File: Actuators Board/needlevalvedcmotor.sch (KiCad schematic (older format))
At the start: 32 parts, among them J10 Conn_01x02_Male, J9 Conn_01x02_Male, Q1 MMDT2222A

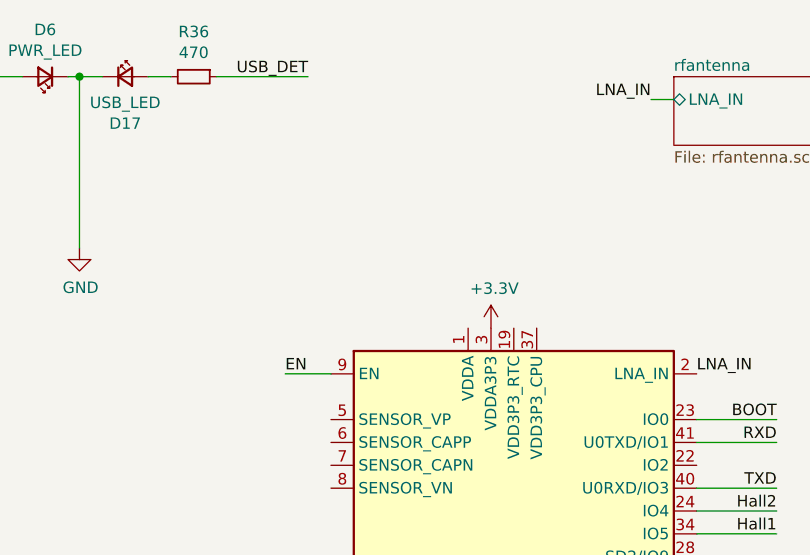
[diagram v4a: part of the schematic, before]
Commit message: Connected 3.3V to ESP32 according to schematic
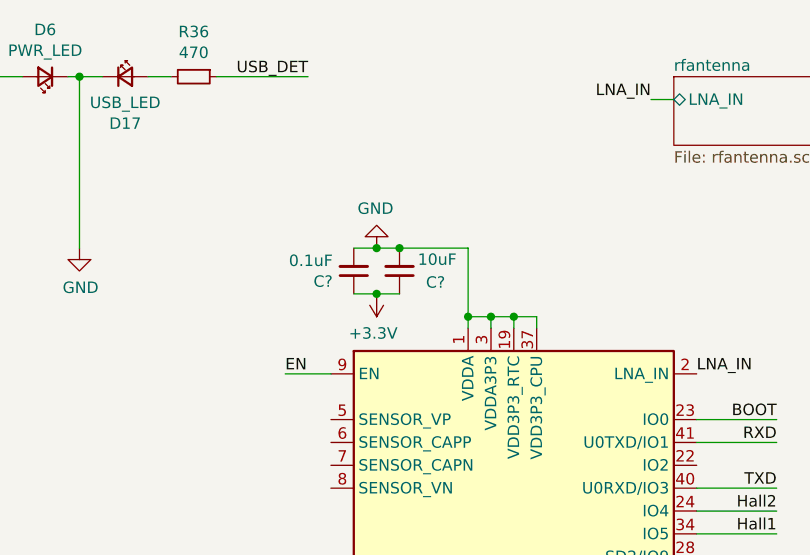
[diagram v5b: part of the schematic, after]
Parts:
- added C?: 10uF, symbol Device:C_Small
- added C?: 0.1uF, symbol Device:C_Small
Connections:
- net +3V3: now also C?.1, C?.1; no longer U?.3 (VDDA3P3), U?.4 (VDDA3P3)
- net GND: now also U?.1 (VDDA), U?.19 (VDD3P3_RTC), U?.3 (VDDA3P3), U?.37 (VDD3P3_CPU), U?.4 (VDDA3P3), U?.43 (VDDA), U?.46 (VDDA), C?.2, C?.2
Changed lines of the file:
@@
 $EndDescr
-$Comp
-L power:+3.3V #PWR020
-U 1 1 5DA60792
-P 4100 1950
-F 0 "#PWR020" H 4100 1800 50  0001 C CNN
-F 1 "+3.3V" H 4115 2123 50  0000 C CNN
-F 2 "" H 4100 1950 50  0001 C CNN
-F 3 "" H 4100 1950 50  0001 C CNN
-	1    4100 1950
-	1    0    0    -1
-$EndComp
 $Comp
 L power:GND #PWR021
@@
 Text Label 4700 6900 0    50   ~ 0
 CAN_RX
+$Comp
+L power:+3.3V #PWR?
+U 1 1 61AA6780
+P 3600 1800
+F 0 "#PWR?" H 3600 1650 50  0001 C CNN
+F 1 "+3.3V" H 3615 1973 50  0000 C CNN
+F 2 "" H 3600 1800 50  0001 C CNN
+F 3 "" H 3600 1800 50  0001 C CNN
+	1    3600 1800
+	-1   0    0    1
+$EndComp
+$Comp
+L Device:C_Small C?
+U 1 1 61AA6786
+P 3700 1700
+F 0 "C?" H 3500 1750 50  0000 L CNN
+F 1 "10uF" H 3450 1650 50  0000 L CNN
+F 2 "" H 3700 1700 50  0001 C CNN
+F 3 "~" H 3700 1700 50  0001 C CNN
+	1    3700 1700
+	-1   0    0    1
+$EndComp
+$Comp
+L Device:C_Small C?
+U 1 1 61AA678C
+P 3500 1700
+F 0 "C?" H 3592 1746 50  0000 L CNN
+F 1 "0.1uF" H 3592 1655 50  0000 L CNN
+F 2 "" H 3500 1700 50  0001 C CNN
+F 3 "~" H 3500 1700 50  0001 C CNN
+	1    3500 1700
+	-1   0    0    1
+$EndComp
+Wire Wire Line
+	3700 1800 3600 1800
+Wire Wire Line
+	3700 1600 3600 1600
+$Comp
+L power:GND #PWR?
+U 1 1 61AA6794
+P 3600 1600
+F 0 "#PWR?" H 3600 1350 50  0001 C CNN
+F 1 "GND" H 3605 1427 50  0000 C CNN
+F 2 "" H 3600 1600 50  0001 C CNN
+F 3 "" H 3600 1600 50  0001 C CNN
+	1    3600 1600
+	-1   0    0    1
+$EndComp
+Connection ~ 3600 1600
+Wire Wire Line
+	3600 1600 3500 1600
+Connection ~ 3600 1800
+Wire Wire Line
+	3600 1800 3500 1800
+Wire Wire Line
+	3700 1600 4000 1600
+Wire Wire Line
+	4000 1600 4000 1900
+Connection ~ 3700 1600
+Wire Wire Line
+	4000 1900 4100 1900
+Wire Wire Line
+	4100 1900 4100 1950
+Connection ~ 4000 1900
+Wire Wire Line
+	4000 1900 4000 1950
+Wire Wire Line
+	4100 1900 4200 1900
+Wire Wire Line
+	4200 1900 4200 1950
+Connection ~ 4100 1900
+Wire Wire Line
+	4200 1900 4300 1900
+Wire Wire Line
+	4300 1900 4300 1950
+Connection ~ 4200 1900
 $EndSCHEMATC

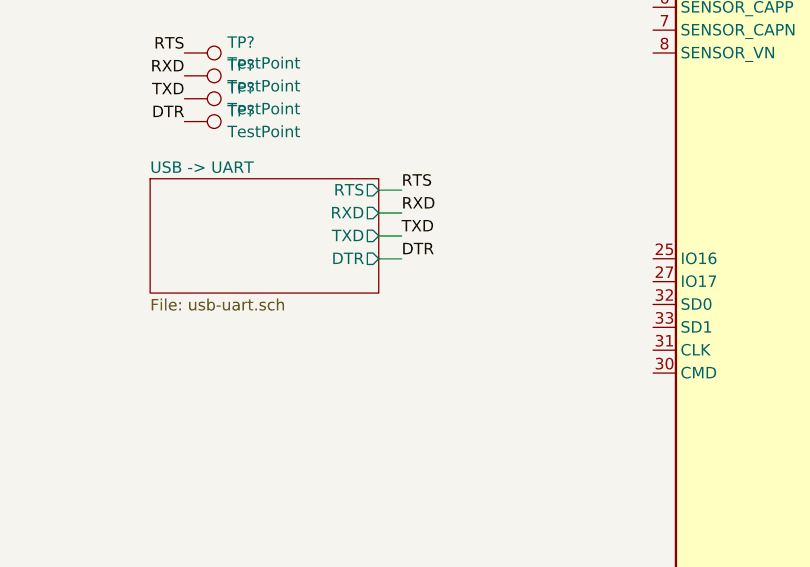
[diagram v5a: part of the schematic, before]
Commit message: Connected 3.3V output from USB-UART converter
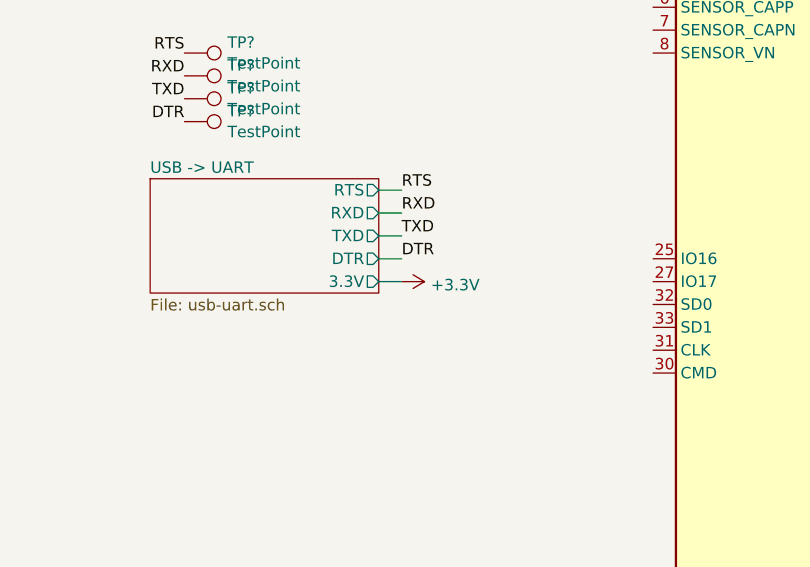
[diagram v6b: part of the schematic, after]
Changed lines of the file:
@@
 F4 "TXD" O R 2200 3450 50
 F5 "DTR" O R 2200 3550 50
+F6 "3.3V" O R 2200 3650 50
 $EndSheet
 $Comp
@@
 	4300 1900 4300 1950
 Connection ~ 4200 1900
+Wire Wire Line
+	2200 3650 2300 3650
+$Comp
+L power:+3.3V #PWR?
+U 1 1 61A70159
+P 2300 3650
+F 0 "#PWR?" H 2300 3500 50  0001 C CNN
+F 1 "+3.3V" V 2315 3778 50  0000 L CNN
+F 2 "" H 2300 3650 50  0001 C CNN
+F 3 "" H 2300 3650 50  0001 C CNN
+	1    2300 3650
+	0    1    1    0
+$EndComp
 $EndSCHEMATC

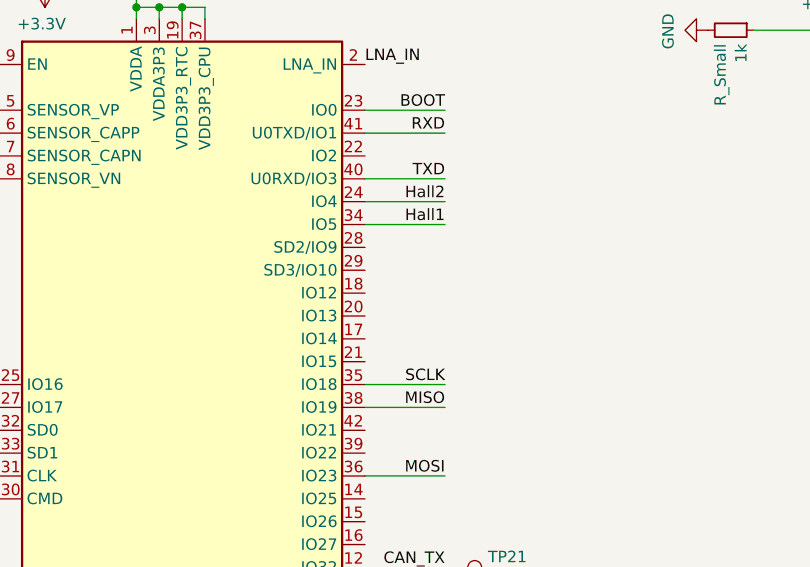
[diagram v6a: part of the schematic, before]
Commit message: Connected H bridge PWM pin to ESP32
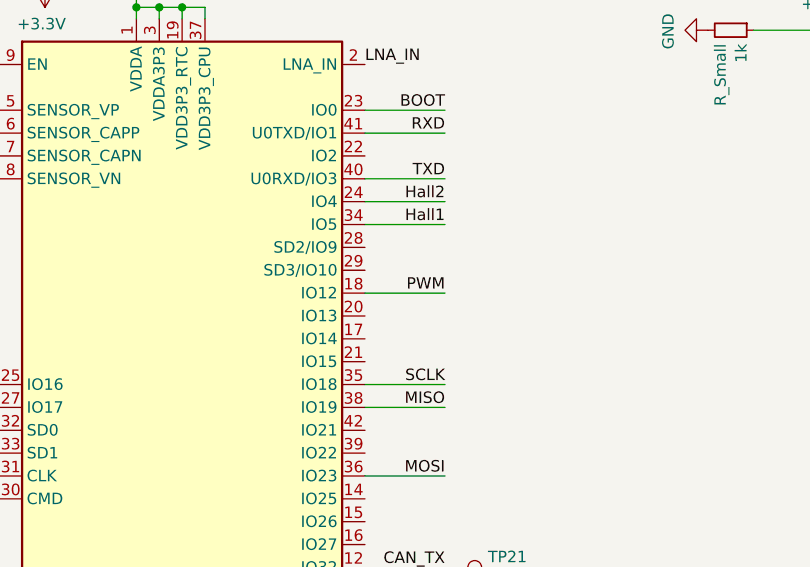
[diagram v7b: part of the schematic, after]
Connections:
- net PWM: now also U?.18 (IO12)
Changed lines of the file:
@@
 	0    1    1    0
 $EndComp
+Wire Wire Line
+	5000 3150 5350 3150
+Text Label 5350 3150 2    50   ~ 0
+PWM
 $EndSCHEMATC

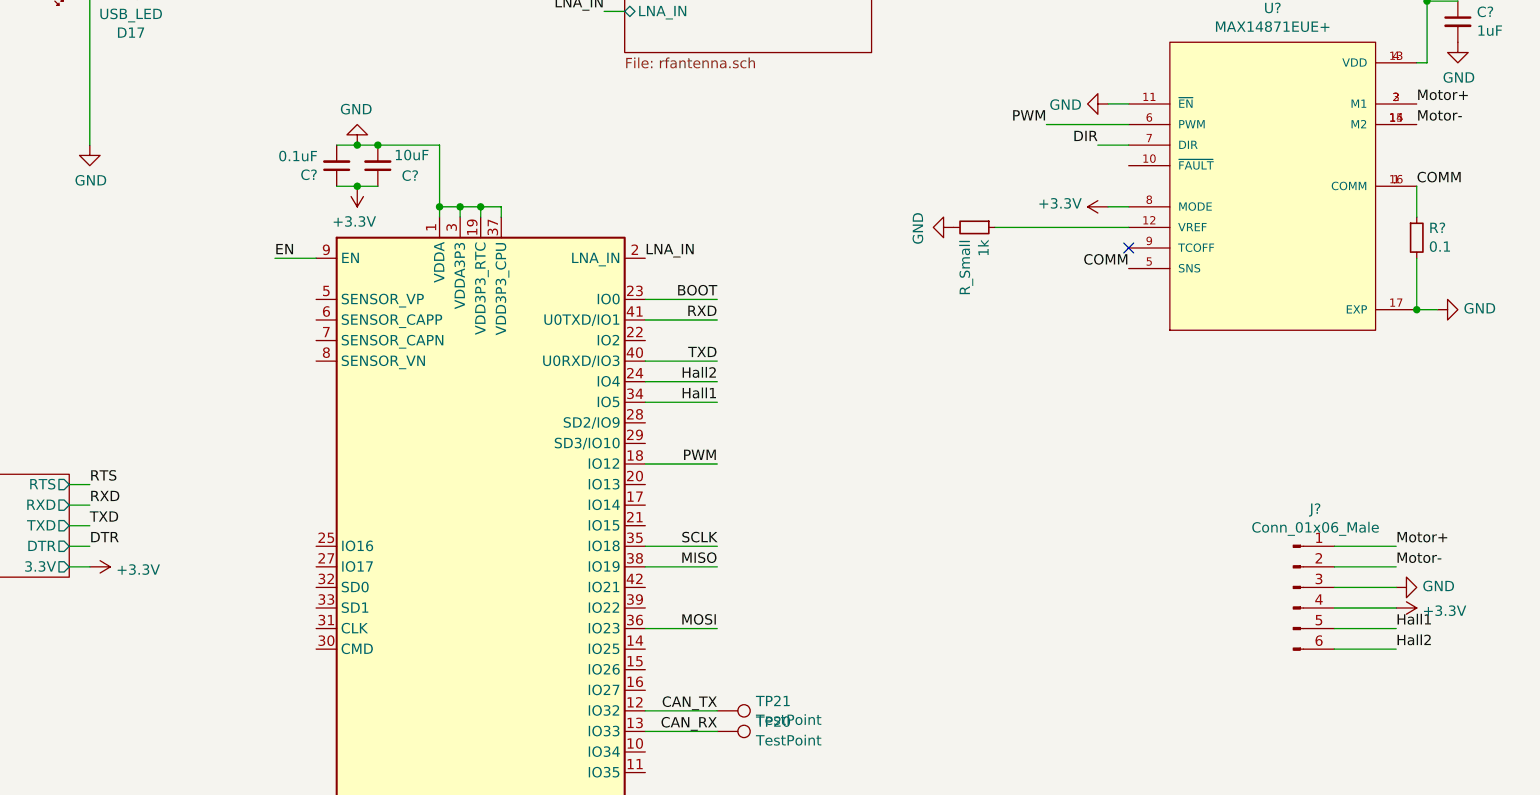
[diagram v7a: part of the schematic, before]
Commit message: Added test points to needle valve motor board
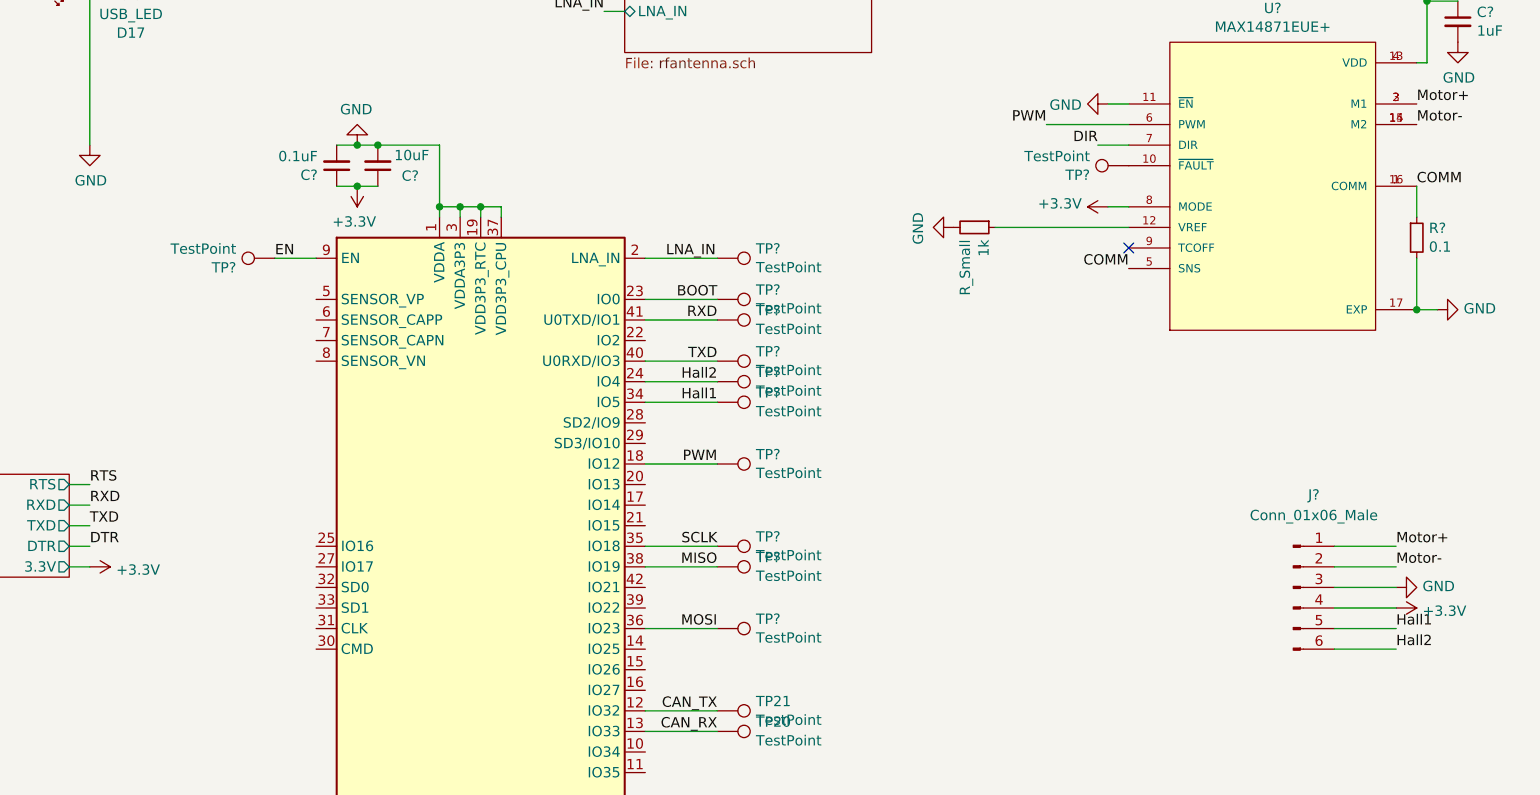
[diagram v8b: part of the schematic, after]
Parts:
- added TP? (x12): TestPoint, symbol Connector:TestPoint
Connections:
- net BOOT: now also TP?.1
- net EN: now also TP?.1
- net Hall1: now also TP?.1
- net Hall2: now also TP?.1
- net LNA_IN: now also TP?.1
- net MISO: now also TP?.1
- net MOSI: now also TP?.1
- net PWM: now also TP?.1
- net RXD: now also TP?.1
- net SCLK: now also TP?.1
- net TXD: now also TP?.1
- net at U?.10 (~FAULT): now also TP?.1
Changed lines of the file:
@@
 U 1 1 6194A5D2
 P 8150 3750
-F 0 "J?" H 8258 4131 50  0000 C CNN
-F 1 "Conn_01x06_Male" H 8258 4040 50  0000 C CNN
+F 0 "J?" H 8250 4200 50  0000 C CNN
+F 1 "Conn_01x06_Male" H 8250 4100 50  0000 C CNN
 F 2 "" H 8150 3750 50  0001 C CNN
 F 3 "~" H 8150 3750 50  0001 C CNN
@@
 Wire Wire Line
 	6700 2000 7350 2000
-Text Label 8650 3550 0    50   ~ 0
-Motor+
 Wire Wire Line
 	8350 3550 8650 3550
@@
 F2 "LNA_IN" B L 4900 950 50
 $EndSheet
-Text Label 5000 2150 0    50   ~ 0
+Text Label 5100 2150 0    50   ~ 0
 LNA_IN
 Text Label 4800 950  2    50   ~ 0
@@
 Text Label 5350 3150 2    50   ~ 0
 PWM
+Text Label 8650 3550 0    50   ~ 0
+Motor+
+$Comp
+L Connector:TestPoint TP?
+U 1 1 61B1B7B5
+P 5350 2350
+F 0 "TP?" V 5304 2538 50  0000 L CNN
+F 1 "TestPoint" V 5395 2538 50  0000 L CNN
+F 2 "" H 5550 2350 50  0001 C CNN
+F 3 "~" H 5550 2350 50  0001 C CNN
+	1    5350 2350
+	0    1    1    0
+$EndComp
+$Comp
+L Connector:TestPoint TP?
+U 1 1 61B1BFB6
+P 5350 2450
+F 0 "TP?" V 5304 2638 50  0000 L CNN
+F 1 "TestPoint" V 5395 2638 50  0000 L CNN
+F 2 "" H 5550 2450 50  0001 C CNN
+F 3 "~" H 5550 2450 50  0001 C CNN
+	1    5350 2450
+	0    1    1    0
+$EndComp
+$Comp
+L Connector:TestPoint TP?
+U 1 1 61B22D1D
+P 5350 2650
+F 0 "TP?" V 5304 2838 50  0000 L CNN
+F 1 "TestPoint" V 5395 2838 50  0000 L CNN
+F 2 "" H 5550 2650 50  0001 C CNN
+F 3 "~" H 5550 2650 50  0001 C CNN
+	1    5350 2650
+	0    1    1    0
+$EndComp
+$Comp
+L Connector:TestPoint TP?
+U 1 1 61B26251
+P 5350 2750
+F 0 "TP?" V 5304 2938 50  0000 L CNN
+F 1 "TestPoint" V 5395 2938 50  0000 L CNN
+F 2 "" H 5550 2750 50  0001 C CNN
+F 3 "~" H 5550 2750 50  0001 C CNN
+	1    5350 2750
+	0    1    1    0
+$EndComp
+$Comp
+L Connector:TestPoint TP?
+U 1 1 61B29519
+P 5350 2850
+F 0 "TP?" V 5304 3038 50  0000 L CNN
+F 1 "TestPoint" V 5395 3038 50  0000 L CNN
+F 2 "" H 5550 2850 50  0001 C CNN
+F 3 "~" H 5550 2850 50  0001 C CNN
+	1    5350 2850
+	0    1    1    0
+$EndComp
+$Comp
+L Connector:TestPoint TP?
+U 1 1 61B2CAF9
+P 5350 3150
+F 0 "TP?" V 5304 3338 50  0000 L CNN
+F 1 "TestPoint" V 5395 3338 50  0000 L CNN
+F 2 "" H 5550 3150 50  0001 C CNN
+F 3 "~" H 5550 3150 50  0001 C CNN
+	1    5350 3150
+	0    1    1    0
+$EndComp
+$Comp
+L Connector:TestPoint TP?
+U 1 1 61B2FF39
+P 5350 3550
+F 0 "TP?" V 5304 3738 50  0000 L CNN
+F 1 "TestPoint" V 5395 3738 50  0000 L CNN
+F 2 "" H 5550 3550 50  0001 C CNN
+F 3 "~" H 5550 3550 50  0001 C CNN
+	1    5350 3550
+	0    1    1    0
+$EndComp
+$Comp
+L Connector:TestPoint TP?
+U 1 1 61B33316
+P 5350 3950
+F 0 "TP?" V 5304 4138 50  0000 L CNN
+F 1 "TestPoint" V 5395 4138 50  0000 L CNN
+F 2 "" H 5550 3950 50  0001 C CNN
+F 3 "~" H 5550 3950 50  0001 C CNN
+	1    5350 3950
+	0    1    1    0
+$EndComp
+$Comp
+L Connector:TestPoint TP?
+U 1 1 61B3A0CE
+P 5350 3650
+F 0 "TP?" V 5304 3838 50  0000 L CNN
+F 1 "TestPoint" V 5395 3838 50  0000 L CNN
+F 2 "" H 5550 3650 50  0001 C CNN
+F 3 "~" H 5550 3650 50  0001 C CNN
+	1    5350 3650
+	0    1    1    0
+$EndComp
+$Comp
+L Connector:TestPoint TP?
+U 1 1 61B41CB9
+P 7350 1700
+F 0 "TP?" V 7304 1888 50  0000 L CNN
+F 1 "TestPoint" V 7395 1888 50  0000 L CNN
+F 2 "" H 7550 1700 50  0001 C CNN
+F 3 "~" H 7550 1700 50  0001 C CNN
+	1    7350 1700
+	0    -1   -1   0
+$EndComp
+$Comp
+L Connector:TestPoint TP?
+U 1 1 61B452FA
+P 3200 2150
+F 0 "TP?" V 3154 2338 50  0000 L CNN
+F 1 "TestPoint" V 3245 2338 50  0000 L CNN
+F 2 "" H 3400 2150 50  0001 C CNN
+F 3 "~" H 3400 2150 50  0001 C CNN
+	1    3200 2150
+	0    -1   -1   0
+$EndComp
+$Comp
+L Connector:TestPoint TP?
+U 1 1 61B4D86B
+P 5350 2150
+F 0 "TP?" V 5304 2338 50  0000 L CNN
+F 1 "TestPoint" V 5395 2338 50  0000 L CNN
+F 2 "" H 5550 2150 50  0001 C CNN
+F 3 "~" H 5550 2150 50  0001 C CNN
+	1    5350 2150
+	0    1    1    0
+$EndComp
+Wire Wire Line
+	5000 2150 5350 2150
 $EndSCHEMATC
